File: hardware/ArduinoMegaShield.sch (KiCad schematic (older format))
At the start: 36 parts, among them P1 CONN_01X02, P10 CONN_01X02, P11 CONN_01X02, P12 CONN_01X02, P13 CONN_01X02, P14 CONN_01X02, P15 CONN_01X02, P16 CONN_01X02, P2 CONN_01X02, P3 CONN_01X02, P4 CONN_01X02, P5 CONN_01X02, P6 CONN_01X02, P7 CONN_01X02, P8 CONN_01X02, P9 CONN_01X02, U1 A4988, U2 A4988, U3 A4988

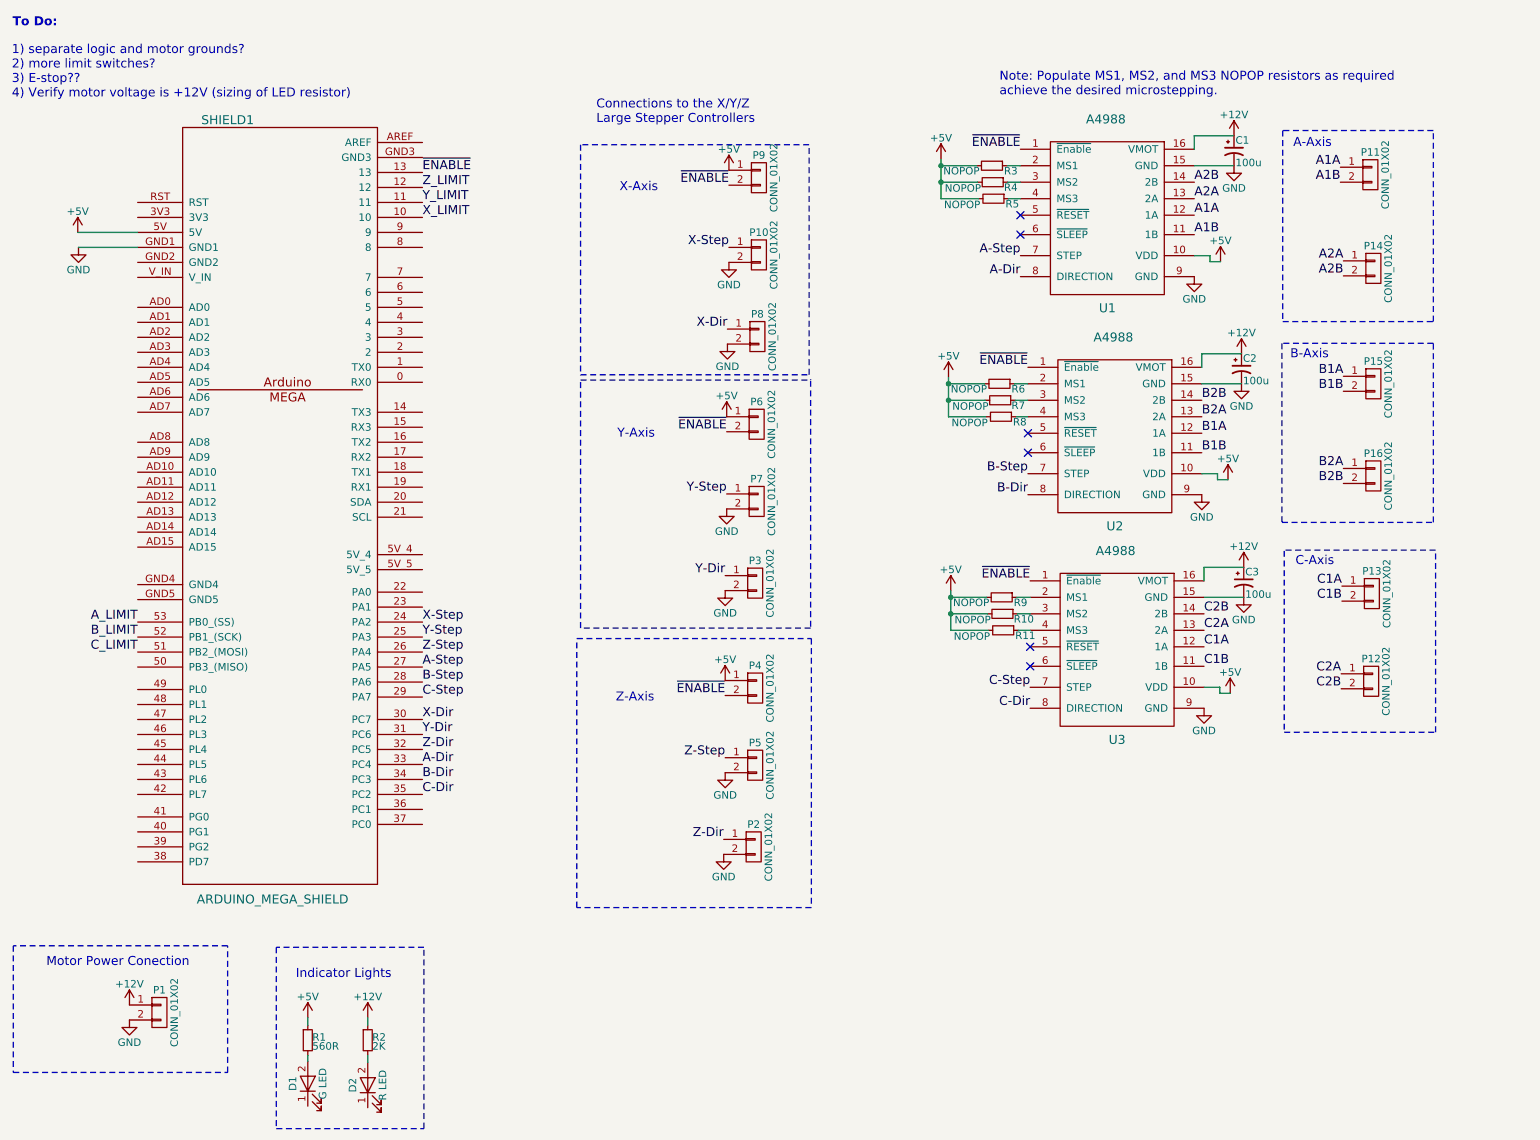
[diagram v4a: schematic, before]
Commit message: added terminal connections for limit switches
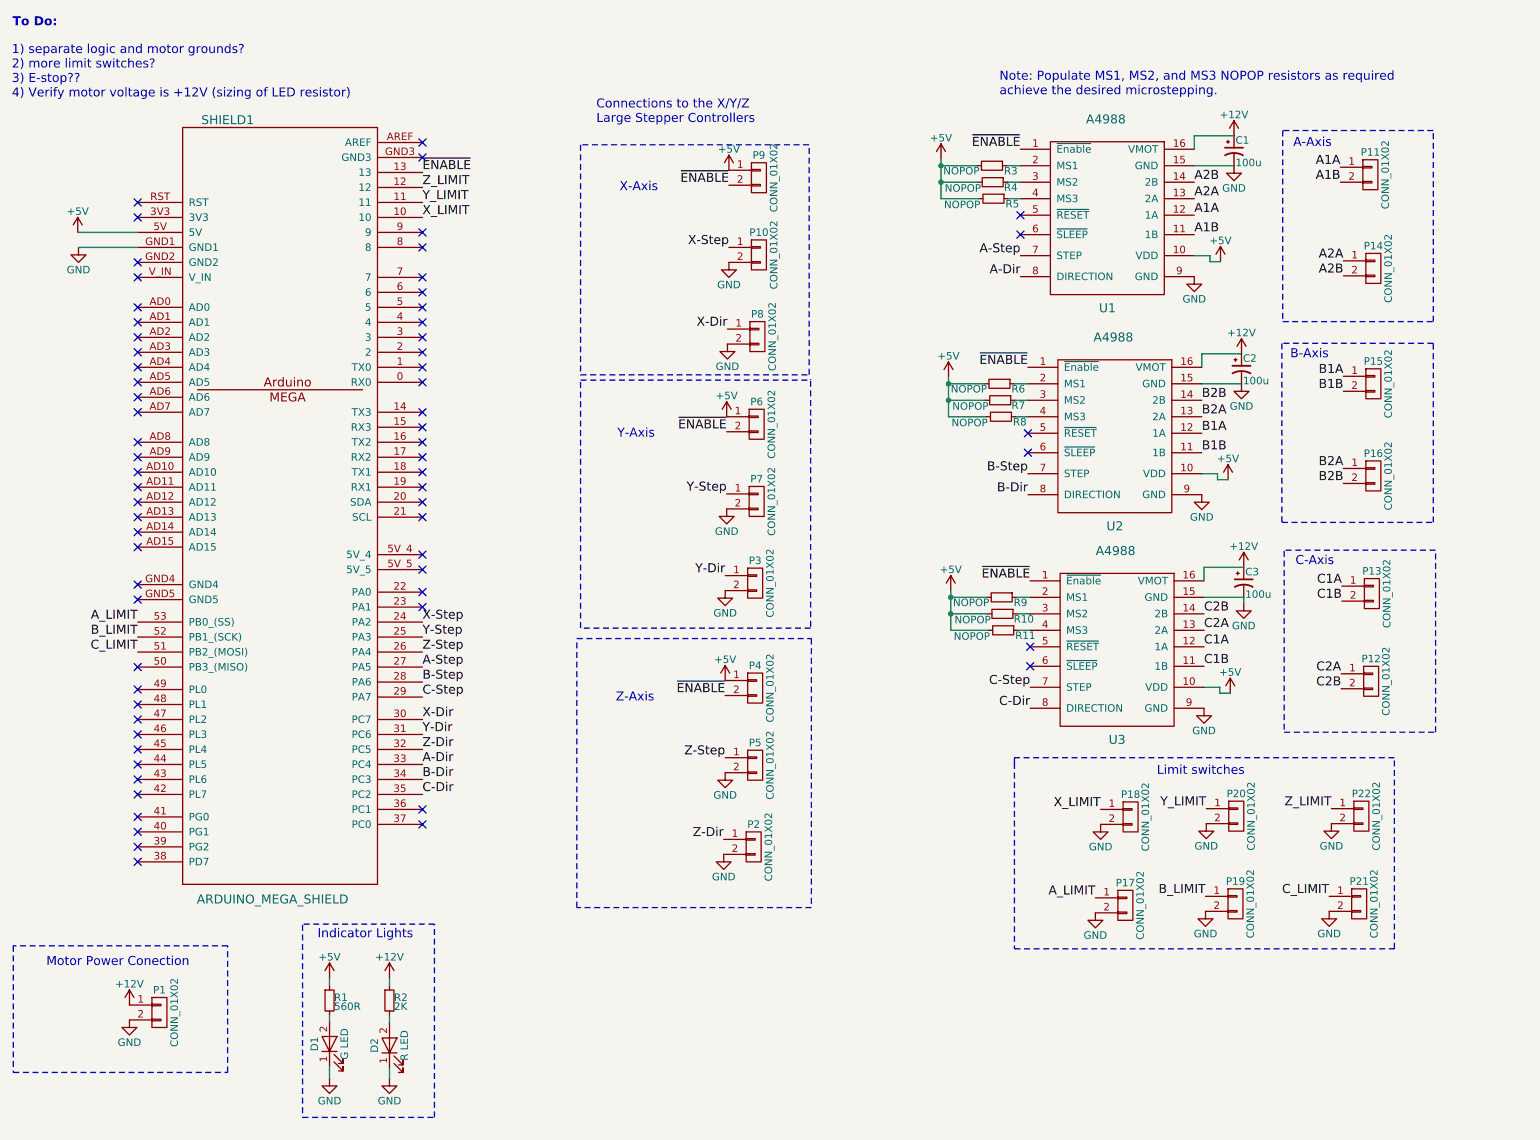
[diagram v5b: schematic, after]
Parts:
- added P17, P18, P19, P20, P21, P22: CONN_01X02, 6axis:Terminal_Block_200_mil, symbol CONN_01X02
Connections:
- net A_LIMIT: now also P17.1 (P1)
- net B_LIMIT: now also P19.1 (P1)
- net C_LIMIT: now also P21.1 (P1)
- net GND: now also D1.1 (K), D2.1 (K), P17.2 (P2), P18.2 (P2), P19.2 (P2), P20.2 (P2), P21.2 (P2), P22.2 (P2)
- net X_LIMIT: now also P18.1 (P1)
- net Y_LIMIT: now also P20.1 (P1)
- net Z_LIMIT: now also P22.1 (P1)
- no-connect marks 6 -> 67
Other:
- note added: "Limit switches"
- moved on the sheet: D1, D2, R1, R2

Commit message: added note about limit switches being on a single bank/port
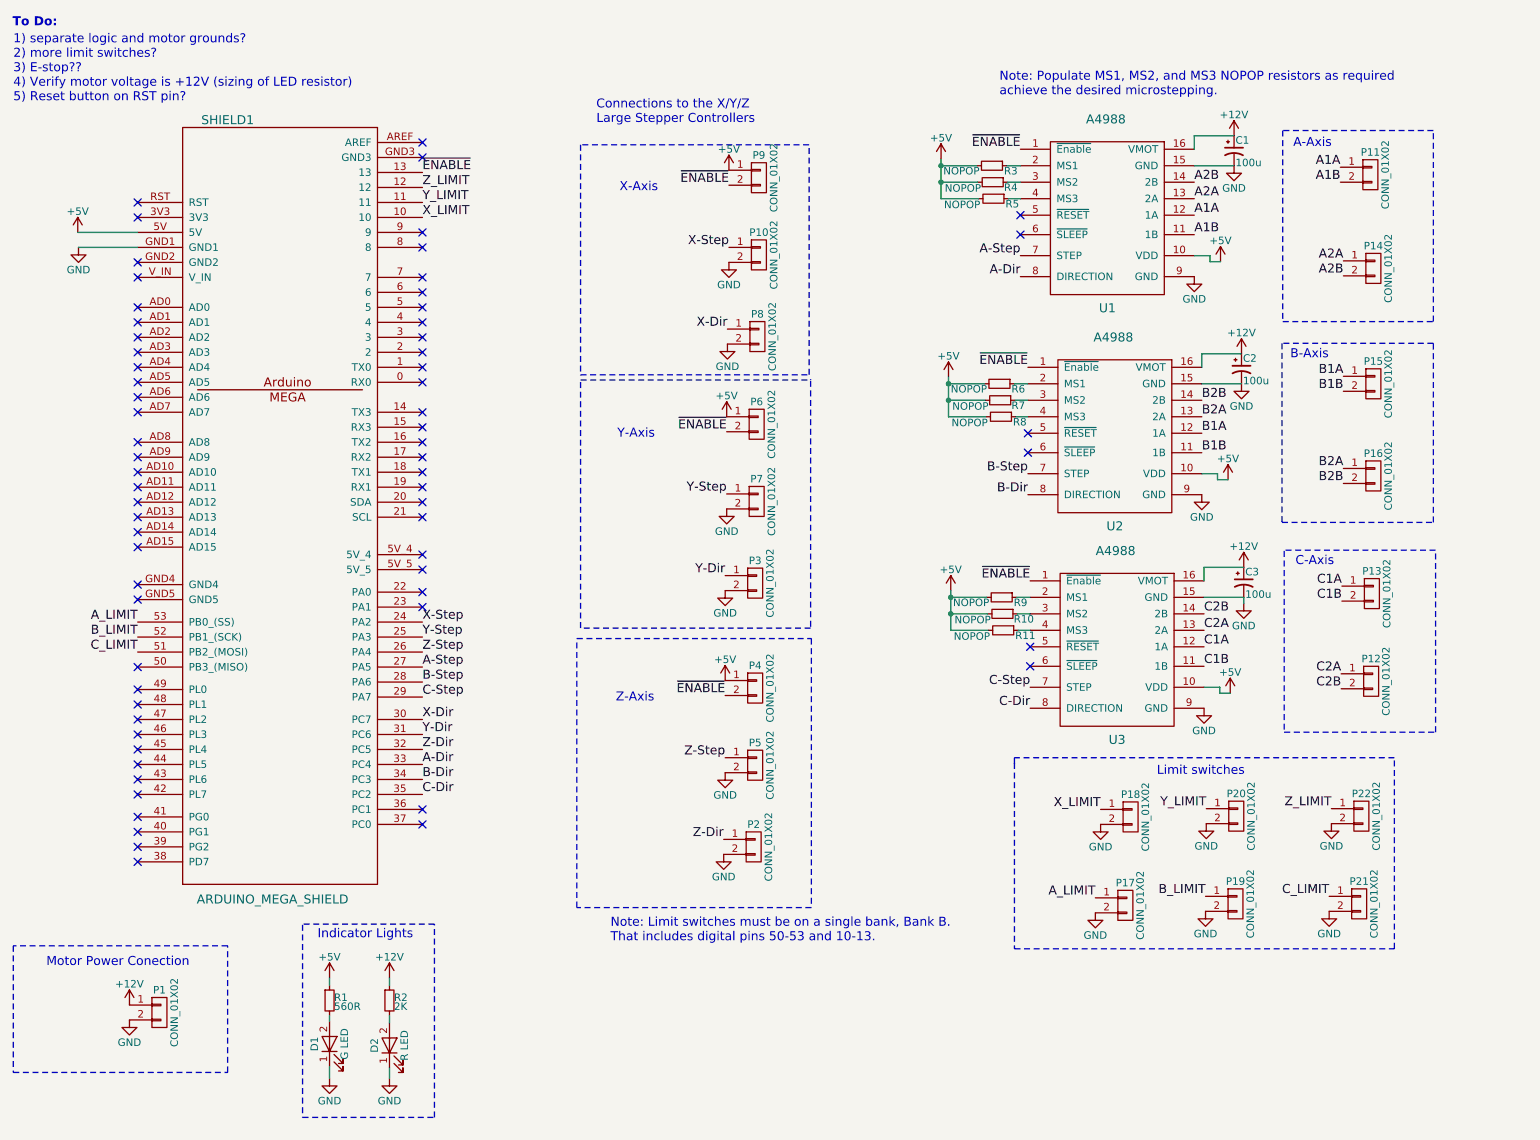
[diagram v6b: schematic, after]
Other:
- note added: "1) separate logic and motor grounds?\n2) more limit switches?\n3) E-stop??\n4) Verify motor voltage is +12V (sizing of LED resistor)\n5) Reset button on RST pin?"
- note added: "Note: Limit switches must be on a single bank, Bank B.\nThat includes digital pins 50-53 and 10-13."
- note removed: "1) separate logic and motor grounds?\n2) more limit switches?\n3) E-stop??\n4) Verify motor voltage is +12V (sizing of LED resistor)"
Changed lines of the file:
@@
 Text Notes 715  565  0    60   ~ 12
 To Do:
-Text Notes 710  1040 0    60   ~ 0
-1) separate logic and motor grounds?\n2) more limit switches?\n3) E-stop??\n4) Verify motor voltage is +12V (sizing of LED resistor)
+Text Notes 720  1065 0    60   ~ 0
+1) separate logic and motor grounds?\n2) more limit switches?\n3) E-stop??\n4) Verify motor voltage is +12V (sizing of LED resistor)\n5) Reset button on RST pin?
 Text Notes 940  6835 0    60   ~ 0
 Motor Power Conection
@@
 Wire Notes Line
 	7400 5435 7400 5480
+Text Notes 4705 6670 0    60   ~ 0
+Note: Limit switches must be on a single bank, Bank B.\nThat includes digital pins 50-53 and 10-13.
 $EndSCHEMATC

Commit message: added NOPOPs for optional pullups on limit switches
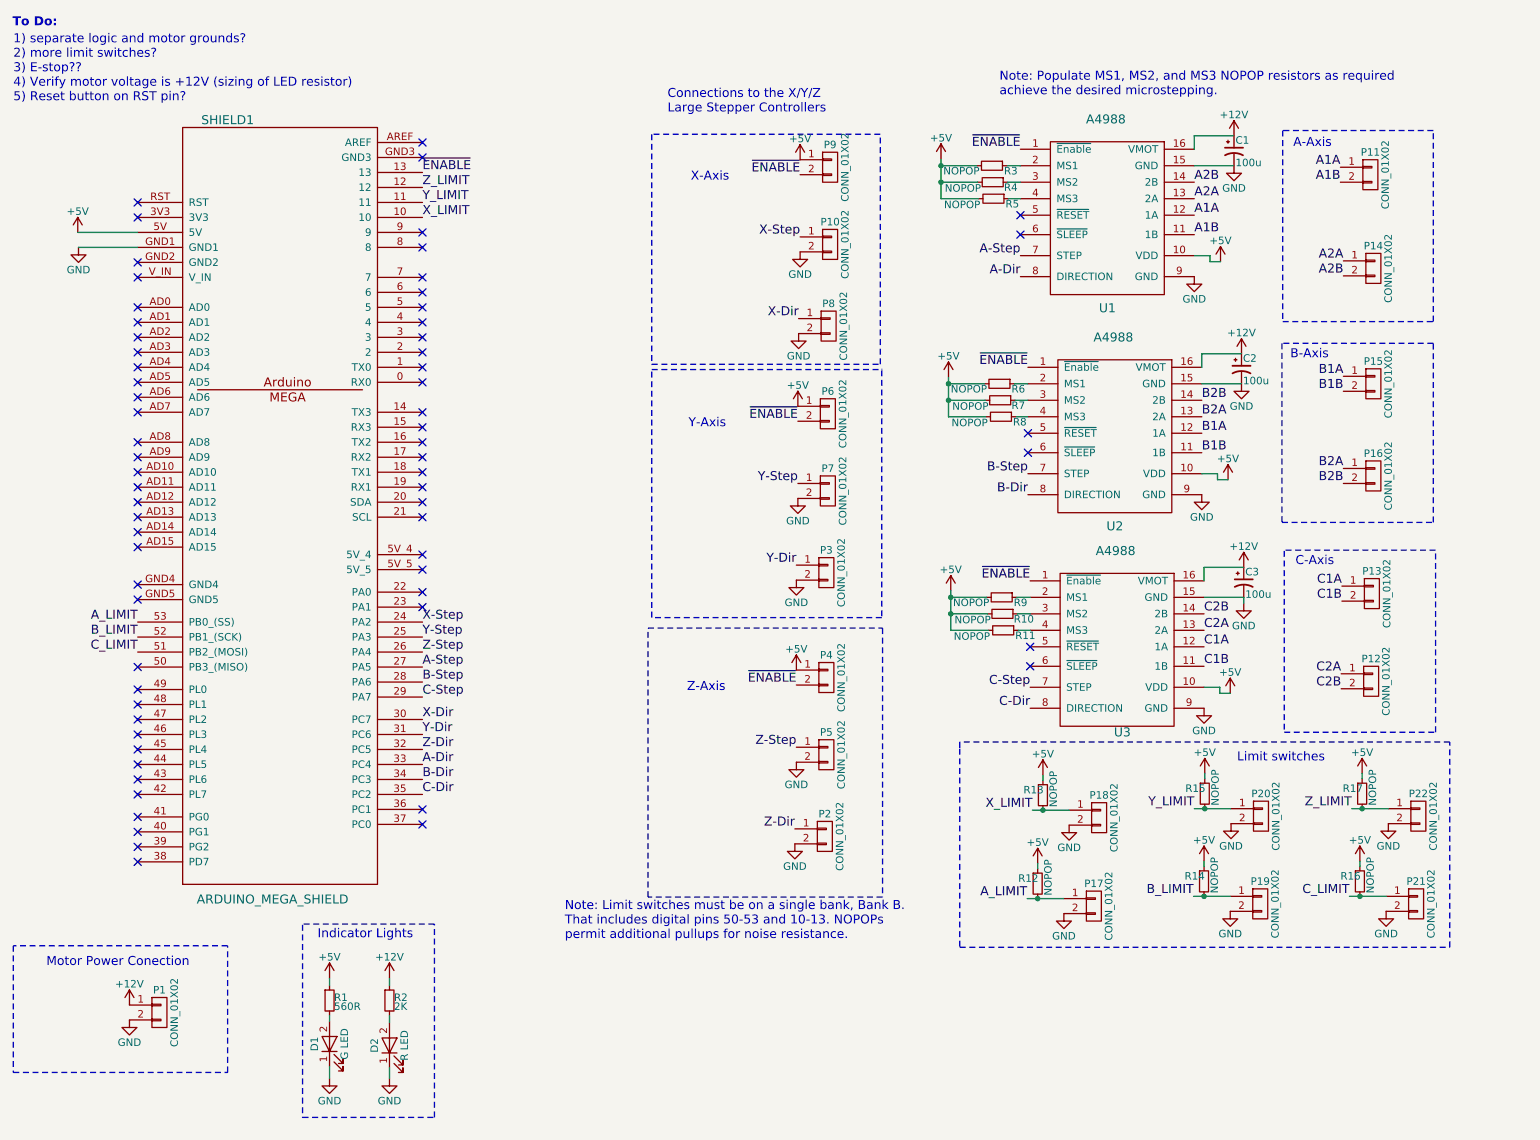
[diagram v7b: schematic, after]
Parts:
- added R12, R13, R14, R15, R16, R17: NOPOP, Resistors_SMD:R_0805_HandSoldering, symbol R_Small
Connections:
- net +5V: now also R12.1, R13.1, R14.1, R15.1, R16.1, R17.1
- net A_LIMIT: now also R12.2
- net B_LIMIT: now also R14.2
- net C_LIMIT: now also R16.2
- net X_LIMIT: now also R13.2
- net Y_LIMIT: now also R15.2
- net Z_LIMIT: now also R17.2
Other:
- note added: "Note: Limit switches must be on a single bank, Bank B.\nThat includes digital pins 50-53 and 10-13. NOPOPs\npermit additional pullups for noise resistance."
- note removed: "Note: Limit switches must be on a single bank, Bank B.\nThat includes digital pins 50-53 and 10-13."
- moved on the sheet: P10, P17, P18, P19, P2, P20, P21, P22, P3, P4, P5, P6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
